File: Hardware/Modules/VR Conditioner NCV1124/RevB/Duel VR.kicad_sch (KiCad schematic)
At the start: 15 parts, among them IC1 NCV1124, J3 Speedy VR Mount

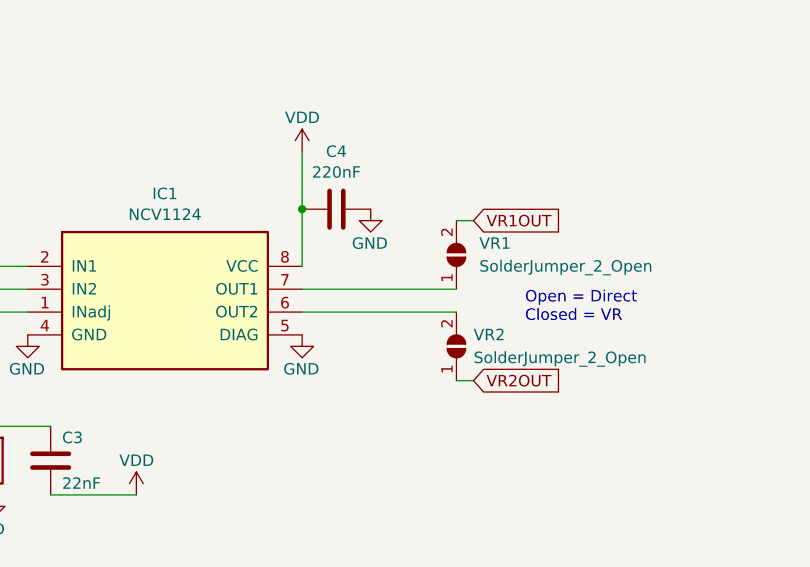
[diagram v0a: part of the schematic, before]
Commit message: VRNCV-B
Layout update. Schematic unchanged.
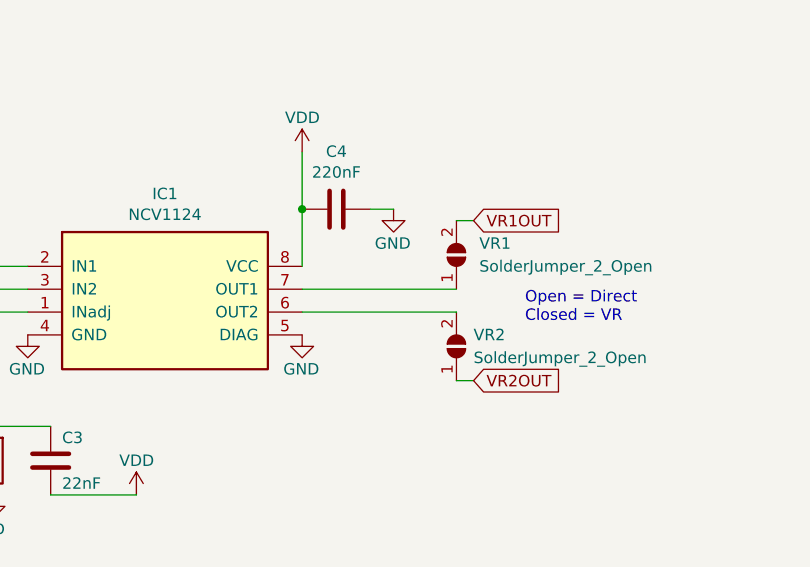
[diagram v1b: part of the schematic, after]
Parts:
- C3: footprint Capacitor_SMD:C_0402_1005Metric -> Capacitor_SMD:C_0603_1608Metric; LCSC C1532 -> C21122
- C4: footprint Capacitor_SMD:C_0805_2012Metric -> Capacitor_SMD:C_0603_1608Metric; LCSC C5378 -> C21120
- R7: footprint Resistor_SMD:R_0402_1005Metric -> Resistor_SMD:R_0603_1608Metric; LCSC C25762 -> C25810
